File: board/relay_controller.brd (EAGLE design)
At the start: 60 x 65 mm, 78 parts, among them IC1 STM32F103C8T, IC3 AT24C, K1 G6K-2F-Y, K2 G6K-2F-Y, K3 G6K-2F-Y, K7 G6K-2F-Y, K8 G6K-2F-Y, Q1 220mA/50V/3.5Ω, Q2 220mA/50V/3.5Ω, Q3 220mA/50V/3.5Ω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

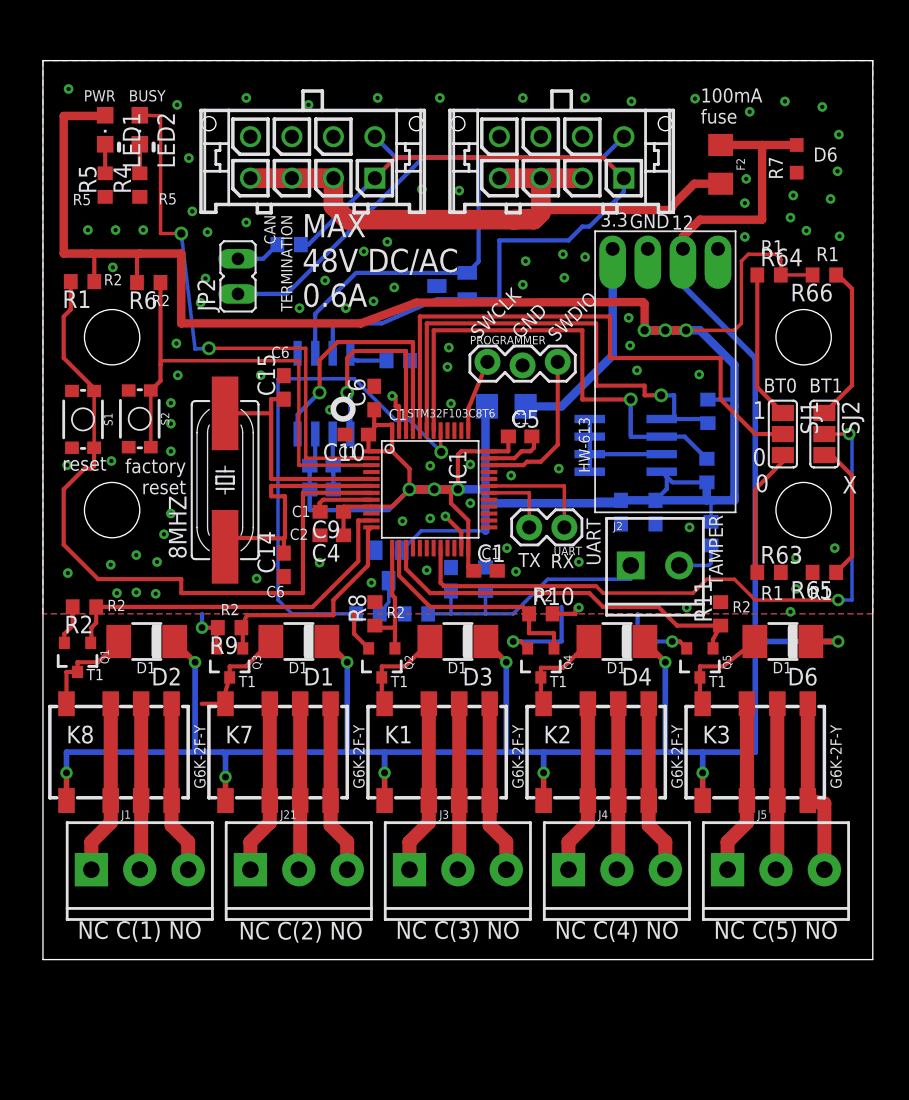
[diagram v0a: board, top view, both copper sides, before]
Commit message: more distance between rj45 connectors
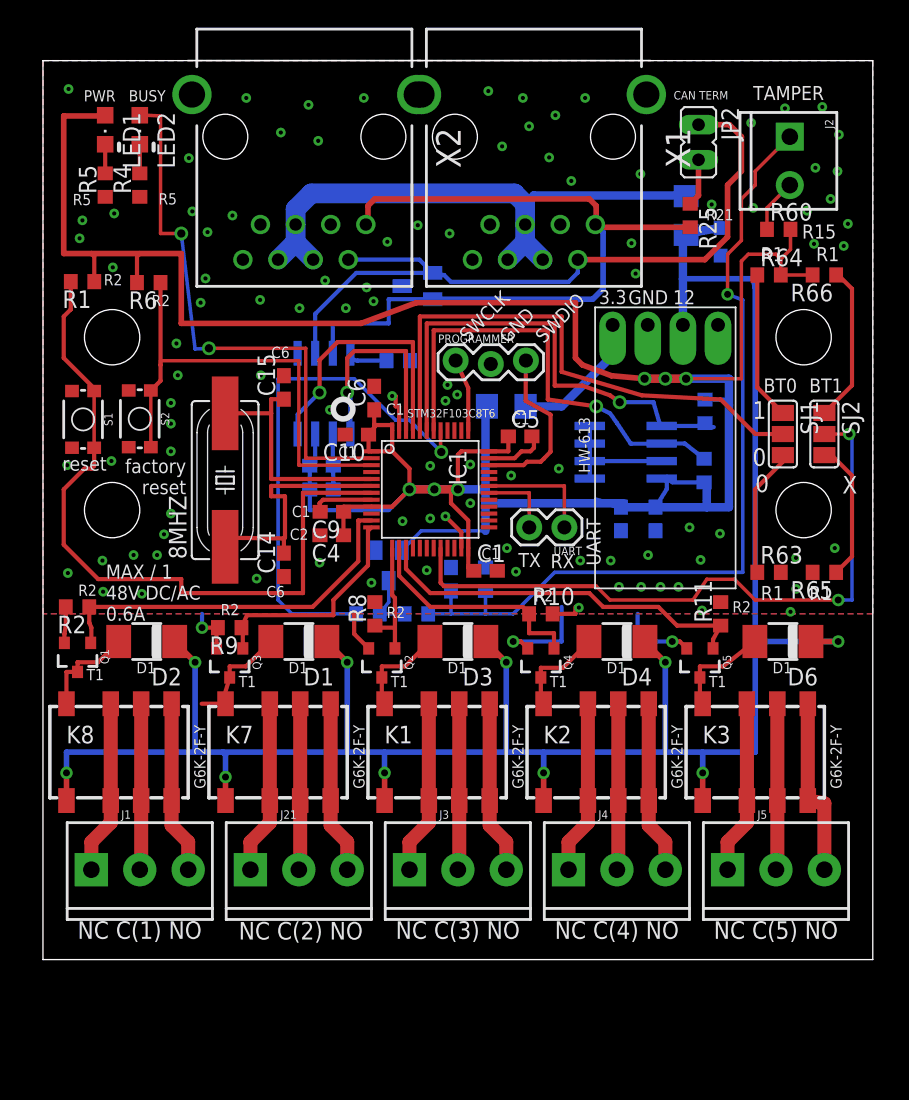
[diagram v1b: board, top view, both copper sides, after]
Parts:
- removed X3, X4: (no value), con-molex-micro-fit-3_0:43045-0812
- added X1, X2: RJ45-8L21-S, con-tycoelectronics:RJ45-SHIELD1
- moved JP2 34.7 mm to (47.4, 59.1), turned to 180 degrees
- moved J2 33.1 mm to (54.0, 59.5), turned to 270 degrees
- moved R25 29.1 mm to (46.8, 53.8), flipped to the top, turned to 270 degrees
- moved R60 22.5 mm to (53.2, 52.8), flipped to the top, turned to 0 degrees
- moved R7 8.14 mm to (49.0, 51.9), flipped to the bottom
- moved U$1 5.50 mm to (45.0, 37.0)
- moved F2 4.47 mm to (46.5, 53.8), flipped to the bottom, turned to 90 degrees
- moved D5 2.50 mm to (27.1, 48.7)
- moved PROGRAMMER 2.30 mm to (29.8, 43.2)
- moved C2 0.50 mm to (41.8, 31.9)
- moved C8 0.50 mm to (44.3, 31.9)
- moved IC3 0.50 mm to (42.1, 36.7)
- moved R2 0.50 mm to (2.50, 25.5)
- moved R27 0.20 mm to (47.9, 39.6)
- moved R3 0.20 mm to (47.8, 35.4)
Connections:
- net CAN_H: now also X1.1, X2.1; no longer X3.P$1, X4.P$1
- net CAN_L: now also X1.2, X2.2; no longer X3.P$5, X4.P$5
- net GND: now also X1.3, X1.7, X1.8, X1.S1, X1.S2, X2.3, X2.7, X2.8, X2.S1, X2.S2; no longer X3.P$6, X3.P$7, X3.P$8, X4.P$6, X4.P$7, X4.P$8
- net PRE_FUSE_12V: now also X1.4, X1.5, X1.6, X2.4, X2.5, X2.6; no longer X3.P$2, X3.P$3, X3.P$4, X4.P$2, X4.P$3, X4.P$4
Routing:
- net N$5: track 20.0 -> 61.4 mm, vias 0 -> 1
- net +12V: track 166.4 -> 158.4 mm
- net CAN_L: track 60.5 -> 53.7 mm
- net PRE_FUSE_12V: track 47.8 -> 41.6 mm
- net N$3: track 15.5 -> 10.0 mm
- net +3V3: track 205.3 -> 210.6 mm
- net I2C1_SCL: track 35.4 -> 33.5 mm
- net I2C1_SDA: track 36.6 -> 34.8 mm
- net BOOT0: track 41.5 -> 39.8 mm
- net CAN_H: track 56.9 -> 55.3 mm
- net SWDIO: track 11.6 -> 12.5 mm
- net BOOT1: track 47.6 -> 48.2 mm
- net GND: track 53.9 -> 53.6 mm, vias 98 -> 103
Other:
- board text added: "CAN TERM"
- board text added: "MAX / 1 48V DC/AC 0.6A"
- board text added: "relay controller 2021.03.11 v1.4"
- board text removed: "CAN TERMINATION"
- board text removed: "MAX 48V DC/AC 0.6A"
- board text removed: "relay controller 2021.03.05 v1.4"

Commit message: fix some labels
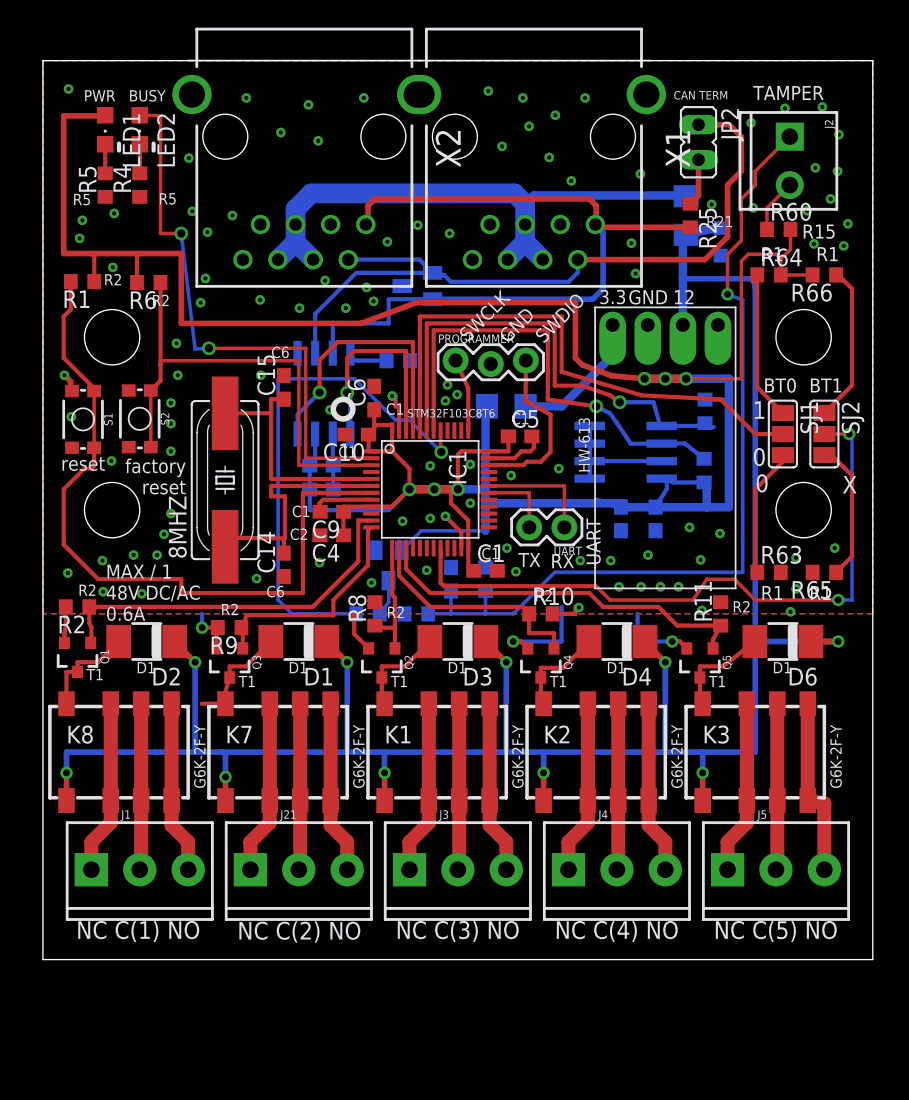
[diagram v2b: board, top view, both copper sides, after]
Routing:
- net GND: track 53.6 -> 54.6 mm, vias 103 -> 104
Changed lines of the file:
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@@
 <wire x1="60" y1="65" x2="0" y2="65" width="0" layer="20"/>
 <wire x1="0" y1="65" x2="0" y2="0" width="0" layer="20"/>
-<text x="36.6" y="41.25" size="1.3" layer="122" rot="MR180">AT24C</text>
+<text x="40.6" y="32.65" size="1.3" layer="122" rot="MR0">AT24C</text>
 <text x="30.7" y="44.6" size="1.016" layer="121" rot="R45">SWCLK</text>
 <text x="33.6" y="44.5" size="1.016" layer="121" rot="R45">GND</text>
@@
 <text x="7.85" y="47.25" size="0.8128" layer="121">R2</text>
 <text x="4.4" y="48.75" size="0.8128" layer="121">R2</text>
-<text x="1.4" y="35.35" size="1.016" layer="121">reset</text>
-<text x="14.15" y="1.45" size="1.27" layer="121">NC C(2) NO</text>
-<text x="2.5" y="1.5" size="1.27" layer="121">NC C(1) NO</text>
+<text x="1.3" y="35.35" size="1.016" layer="121">reset</text>
+<text x="14.05" y="1.45" size="1.27" layer="121">NC C(2) NO</text>
+<text x="2.4" y="1.5" size="1.27" layer="121">NC C(1) NO</text>
 <circle x="24" y="38.5" radius="0.5" width="0.4064" layer="122"/>
 <wire x1="37.5" y1="39.5" x2="37.5" y2="35" width="0.254" layer="122"/>
@@
 <text x="22.85" y="34.15" size="1.016" layer="122" rot="MR180">C2</text>
 <text x="22.85" y="36.15" size="1.016" layer="122" rot="MR180">C1</text>
-<text x="44.85" y="31.15" size="1.016" layer="122" rot="MR180">C1</text>
-<text x="39.85" y="31.15" size="1.016" layer="122" rot="MR180">C2</text>
+<text x="44.45" y="29.95" size="1.016" layer="122" rot="MR180">C1</text>
+<text x="41.55" y="29.95" size="1.016" layer="122" rot="MR180">C2</text>
 <text x="47.85" y="42.15" size="1.016" layer="122" rot="MR180">R1</text>
 <text x="48.05" y="37.95" size="1.016" layer="122" rot="MR180">R1</text>
@@
 <text x="31.25" y="30.3" size="1.016" layer="122" rot="MR180">R2</text>
 <text x="57.35" y="53.15" size="1.016" layer="121" rot="R180">R15</text>
-<text x="49.7" y="48.7" size="1.016" layer="122" rot="MR0">D6</text>
+<text x="49.8" y="49" size="1.016" layer="122" rot="MR0">D6</text>
 <text x="39.3" y="31.9" size="1.016" layer="121" rot="R270">UART</text>
 <text x="36.7" y="28.3" size="1.016" layer="121">RX</text>
@@
 <text x="51.9" y="50.5" size="1.016" layer="121">R1</text>
 <text x="49.55" y="62.8" size="0.6096" layer="121" rot="R180">CAN TERM</text>
-<text x="47.95" y="53.45" size="0.8128" layer="121">R21</text>
+<text x="47.95" y="52.95" size="0.8128" layer="121">R21</text>
 <text x="25.5" y="1.5" size="1.27" layer="121">NC C(3) NO</text>
 <text x="37" y="1.5" size="1.27" layer="121">NC C(4) NO</text>
@@
 <via x="2.65" y="52.15" extent="1-16" drill="0.3"/>
 <via x="9.25" y="32.25" extent="1-16" drill="0.3"/>
-<via x="1.75" y="35.75" extent="1-16" drill="0.3"/>
+<via x="1.55" y="42.25" extent="1-16" drill="0.3"/>
 <via x="4.95" y="36.05" extent="1-16" drill="0.3"/>
 <via x="8.75" y="30.75" extent="1-16" drill="0.3"/>
@@
 <via x="45.95" y="26.95" extent="1-16" drill="0.3"/>
 <via x="44.65" y="26.95" extent="1-16" drill="0.3"/>
+<via x="2.05" y="39.25" extent="1-16" drill="0.3"/>
+<wire x1="1.55" y1="42.25" x2="2" y2="41.8" width="0.4064" layer="1"/>
+<wire x1="2" y1="41.8" x2="2" y2="41.5" width="0.4064" layer="1"/>
 </signal>
 <signal name="+3V3">

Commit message: change to packages with place drawing
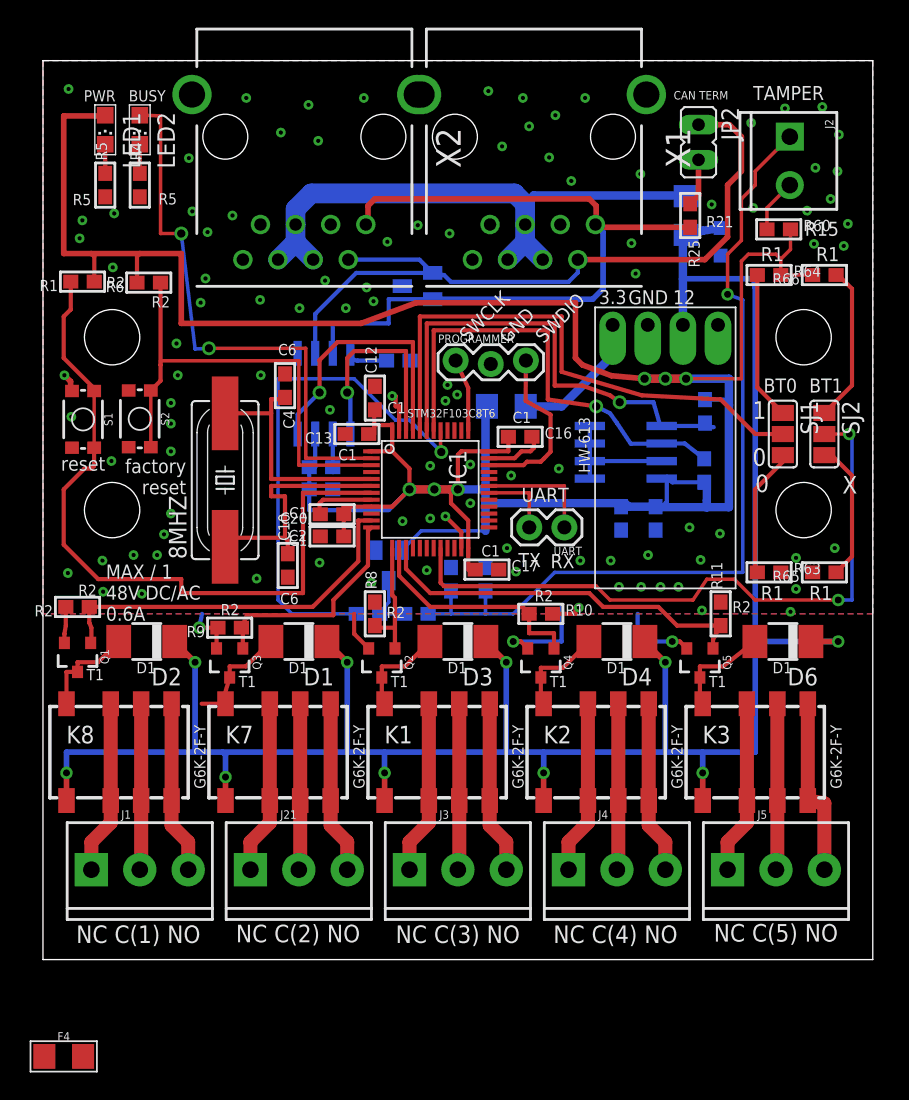
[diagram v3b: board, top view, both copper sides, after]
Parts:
- removed C11: 10nF, eagle-ltspice:C0603
- removed C14, C15: 33p, rcl:C0603
- removed C3, C8: 100n, rcl:C0603
- removed C7: 1u, rcl:C0603
- added C12, C13, C16, C17, C19, C20: 100n, microbuilder:0603
- added F4: 6V/0.5A, SparkFun-Fuses:1206
- C1, C5, C6: value 100n -> 1u; device rcl:C0603 -> microbuilder:0603
- C10: value 100n -> 33pf; device rcl:C0603 -> microbuilder:0603
- C2: value 1u -> 10nF; device rcl:C0603 -> microbuilder:0603
- C4: value 1u -> 33pf; device rcl:C0603 -> microbuilder:0603
- C9: device rcl:C0603 -> microbuilder:0603
- F2: value 12V/50mA -> 6V/0.5A
- R1, R10, R11, R2, R24, R25, R27, R3, R4, R5, R59, R6, R60, R61, R62, R63, R64, R65, R66, R8, R9: device rcl:R0603 -> microbuilder:0603
- moved C2 13.0 mm to (29.5, 27.5)
- moved C1 11.4 mm to (20.9, 30.6), turned to 180 degrees
- moved C4 11.3 mm to (17.5, 41.5), turned to 270 degrees
- moved C10 10.7 mm to (17.7, 28.5), turned to 90 degrees
- moved C5 9.41 mm to (41.8, 31.9), flipped to the bottom, turned to 270 degrees
- moved C6 6.31 mm to (20.1, 35.6), flipped to the bottom, turned to 180 degrees
- moved C9 1.80 mm to (20.1, 34.0), flipped to the bottom
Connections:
- net +3V3: now also C12.1, C13.1, C16.1, C17.1, C19.1, C20.1; no longer C10.1, C2.1, C3.1, C4.1, C7.1, C8.1
- net GND: now also C10.1, C12.2, C13.2, C16.2, C17.2, C19.2, C2.1, C20.2, C4.1; no longer C10.2, C11.1, C14.1, C15.2, C2.2, C3.2, C4.2, C7.2, C8.2
- net N$1: now also C4.2; no longer C15.1
- net N$2: now also C10.2; no longer C14.2
- net N$5: now also C2.2; no longer C11.2
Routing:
- net GND: track 54.6 -> 52.1 mm
- net +3V3: track 210.6 -> 208.6 mm

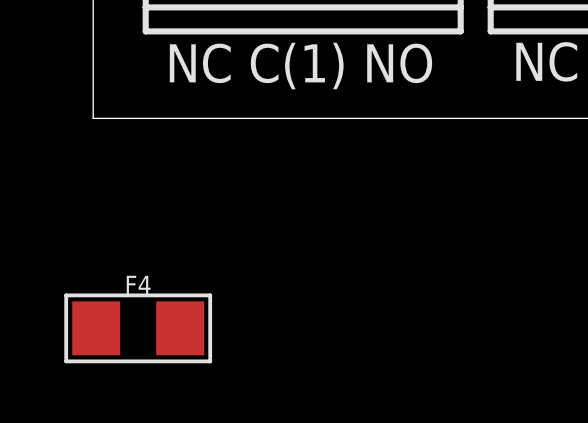
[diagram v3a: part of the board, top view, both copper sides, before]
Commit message: remove unused fuse
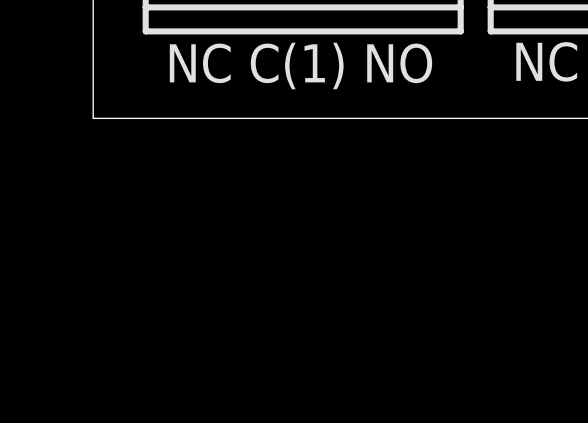
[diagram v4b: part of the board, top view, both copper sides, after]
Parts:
- removed F4: 6V/0.5A, SparkFun-Fuses:1206
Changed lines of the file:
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@@
 <element name="C10" library="microbuilder" package="0603" value="33pf" x="17.7" y="28.5" rot="R90"/>
 <element name="C2" library="microbuilder" package="0603" value="10nF" x="29.5" y="27.5" rot="MR270"/>
-<element name="F4" library="SparkFun-Fuses" package="1206" value="6V/0.5A" x="1.5" y="-7">
-<attribute name="PROD_ID" value="RES-08585" x="1.5" y="-7" size="1.778" layer="27" display="off"/>
-</element>
 </elements>
 <signals>
